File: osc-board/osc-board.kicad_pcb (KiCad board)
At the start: 4 copper layers, 68 parts, among them J1 01x20, J2 01x20, Q1 MMBT3906, Q2 MMBT3906, SW1 SW_DIP_x02, SW2 SW_DIP_x02, U1 LM13700, U2 TL074, U3 TL074

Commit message: wip pre-redo orientation
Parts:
- removed SW1, SW2: SW_DIP_x02, Button_Switch_SMD:SW_DIP_SPSTx02_Slide_Omron_A6S-210x_W8.9mm_P2.54mm
- added J3: Conn_01x03_Female, Connector_PinHeader_2.54mm:PinHeader_1x03_P2.54mm_Vertical, F.Cu at (91.1, 76.6)
- added J4: Conn_01x03_Female, Connector_PinHeader_2.54mm:PinHeader_1x03_P2.54mm_Vertical, F.Cu at (92.1, 110.8)
- moved R24 173.6 mm to (54.2, 112.1), turned to 180 degrees
- moved C10 158.2 mm to (60.8, 108.8), turned to 180 degrees
- moved R26 155.4 mm to (54.2, 115.1), turned to 180 degrees
- moved R2 153.4 mm to (60.8, 111.6)
- moved R4 152.4 mm to (54.2, 109.2), turned to 180 degrees
- moved R22 146.2 mm to (63.8, 102.7), turned to 180 degrees
- moved R19 143.2 mm to (94.1, 122.2), turned to 180 degrees
- moved U3 137.9 mm to (99.8, 112.9), turned to -90 degrees
- moved RV2 136.7 mm to (107.3, 96.3)
- moved R16 130.7 mm to (94.1, 125.0)
- moved R20 119.8 mm to (100.1, 120.9), turned to 180 degrees
- moved Q2 117.9 mm to (108.1, 112.4), turned to 90 degrees
- moved C2 112.6 mm to (103.9, 107.2)
- moved C14 108.8 mm to (99.6, 107.2), turned to 180 degrees
- moved C4 107.9 mm to (95.4, 107.2), turned to 180 degrees
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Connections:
- U1 pad 1: /Osc2_Iabc -> /Osc1_Iabc
- U1 pad 12: /Osc1_Integr_In -> /Osc2_Integr_In
- U1 pad 13: Net-(R1-Pad1) -> Net-(R2-Pad1)
- U1 pad 16: /Osc1_Iabc -> /Osc2_Iabc
- U1 pad 4: Net-(R2-Pad1) -> Net-(R1-Pad1)
- U1 pad 5: /Osc2_Integr_In -> /Osc1_Integr_In
- U3 pad 10: /+4.5V -> Net-(R32-Pad2)
- U3 pad 5: Net-(R32-Pad2) -> /+4.5V
- U3 pad 6: Net-(R30-Pad1) -> /Osc2_Integr_In
- U3 pad 7: Net-(R36-Pad1) -> /Osc2_Integr_Out
- U3 pad 8: /Osc2_Integr_Out -> Net-(R36-Pad1)
- U3 pad 9: /Osc2_Integr_In -> Net-(R30-Pad1)

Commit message: wip
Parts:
- moved C5 50.4 mm to (50.3, 56.0)
- moved C6 50.4 mm to (50.3, 58.8)
- moved C9 50.4 mm to (58.9, 56.0)
- moved R1 50.4 mm to (54.6, 58.9)
- moved R17 50.4 mm to (58.8, 58.9)
- moved R18 50.4 mm to (63.1, 58.9)
- moved R21 50.4 mm to (63.1, 56.0)
- moved R23 50.4 mm to (67.3, 58.9)
- moved R25 50.4 mm to (67.3, 61.7)
- moved R3 50.4 mm to (54.6, 61.7)
- moved R35 32.8 mm to (112.1, 46.6)
- moved C13 21.9 mm to (113.0, 57.1)
- moved Q1 20.5 mm to (108.1, 87.2)
- moved R13 20.5 mm to (103.5, 91.4), turned to 0 degrees
- moved R11 17.3 mm to (108.1, 91.4), turned to 0 degrees
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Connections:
- U2 pad 1: Net-(Q1-Pad1) -> Net-(R35-Pad1)
- U2 pad 12: Net-(R18-Pad2) -> /+4.5V
- U2 pad 13: Net-(R17-Pad2) -> Net-(C1-Pad1)
- U2 pad 14: /Osc1_FB -> Net-(Q1-Pad1)
- U2 pad 2: Net-(C1-Pad1) -> Net-(R27-Pad1)
- U2 pad 3: /+4.5V -> Net-(R29-Pad2)
- U2 pad 5: Net-(R29-Pad2) -> Net-(R18-Pad2)
- U2 pad 6: Net-(R27-Pad1) -> Net-(R17-Pad2)
- U2 pad 7: Net-(R35-Pad1) -> /Osc1_FB

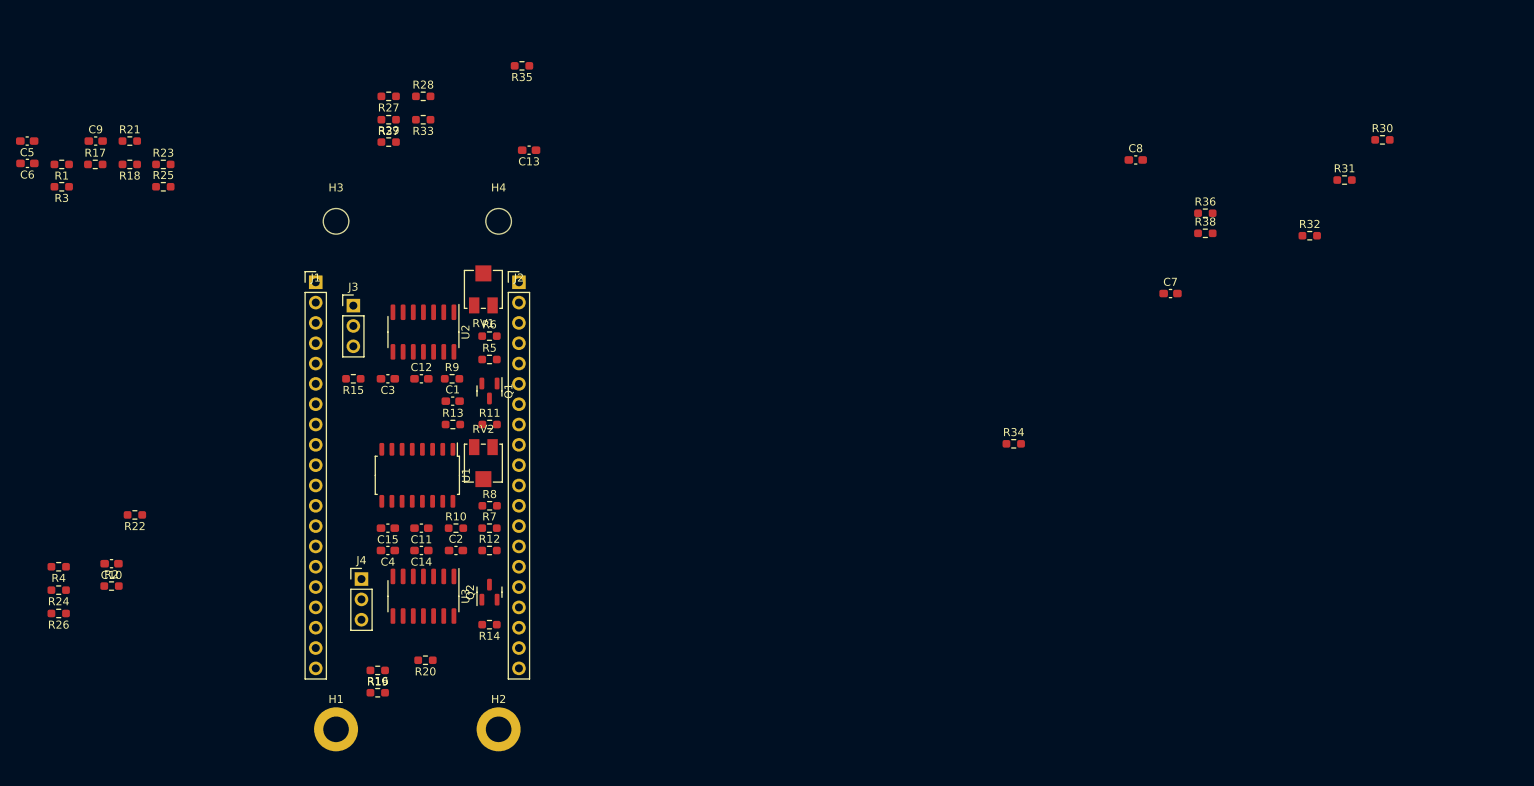
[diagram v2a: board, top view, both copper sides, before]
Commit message: OSC board layout done
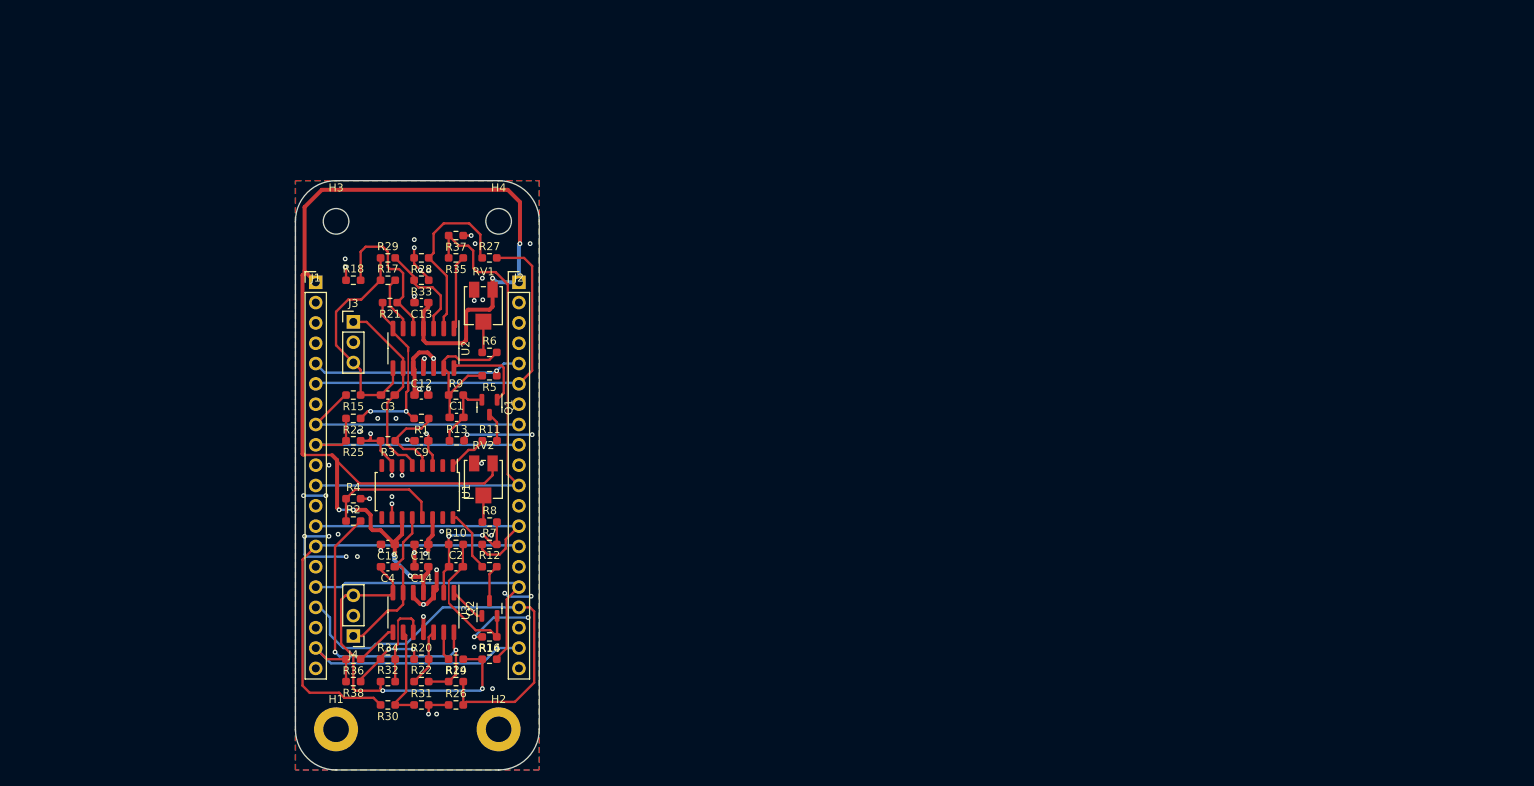
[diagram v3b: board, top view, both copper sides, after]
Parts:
- removed C10, C6, C8: 100n, Capacitor_SMD:C_0603_1608Metric_Pad1.08x0.95mm_HandSolder
- removed C5, C7: 1u, Capacitor_SMD:C_0603_1608Metric_Pad1.08x0.95mm_HandSolder
- moved R30 143.0 mm to (95.4, 126.5), turned to 180 degrees
- moved R31 132.7 mm to (99.6, 126.5)
- moved R32 128.0 mm to (95.4, 123.6)
- moved R38 120.3 mm to (91.1, 123.6), turned to 180 degrees
- moved R36 120.2 mm to (91.1, 120.8), turned to 180 degrees
- moved R34 82.7 mm to (95.4, 120.8)
- moved C9 55.3 mm to (99.6, 93.5), turned to 180 degrees
- moved R1 55.0 mm to (99.6, 90.7)
- moved R3 51.7 mm to (95.4, 93.5)
- moved R24 51.0 mm to (103.9, 123.6), turned to 0 degrees
- moved R26 51.0 mm to (103.9, 126.5), turned to 0 degrees
- moved R22 41.4 mm to (99.6, 123.6), turned to 0 degrees
- moved R23 39.6 mm to (91.1, 90.7), turned to 180 degrees
- moved R25 39.6 mm to (91.1, 93.5), turned to 180 degrees
- moved R17 39.3 mm to (95.4, 73.4)
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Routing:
- net /+9V: track 0.00 -> 153.3 mm, vias 0 -> 6
- net /+4.5V: track 0.00 -> 95.9 mm, vias 0 -> 30
- net /Osc1_PWM_Out: track 0.00 -> 65.1 mm
- net /Osc2_Sq_Out: track 0.00 -> 54.8 mm
- net /Osc2_CV_PWM: track 0.00 -> 54.4 mm
- net /Osc2_Integr_Out: track 0.00 -> 46.1 mm, vias 0 -> 2
- net /Osc1_CV_PWM: track 0.00 -> 45.8 mm
- net /Osc2_FB: track 0.00 -> 42.5 mm, vias 0 -> 2
- net /Osc2_Tri_Out: track 0.00 -> 36.0 mm
- net /Osc2_PWM_Out: track 0.00 -> 34.1 mm
- net /Osc2_CV_Freq: track 0.00 -> 33.0 mm
- net /Osc1_Sq_Out: track 0.00 -> 32.2 mm
- net /Osc1_Tri_Out: track 0.00 -> 30.7 mm
- net /Osc1_Integr_Out: track 0.00 -> 28.2 mm
- net /Osc1_CV_Freq: track 0.00 -> 27.0 mm, vias 0 -> 1
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- added copper zone on B.Cu, net /+4.5V
- added copper zone on F.Cu, net /+4.5V
- added copper zone on In1.Cu, net /GND
- added copper zone on In2.Cu, net /GND
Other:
- board outline added: 30.5 x 73.7 mm
